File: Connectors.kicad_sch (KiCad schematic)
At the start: 13 parts, among them J4 Conn_01x06, J5 Conn_01x06, U10 TJA1051T/3

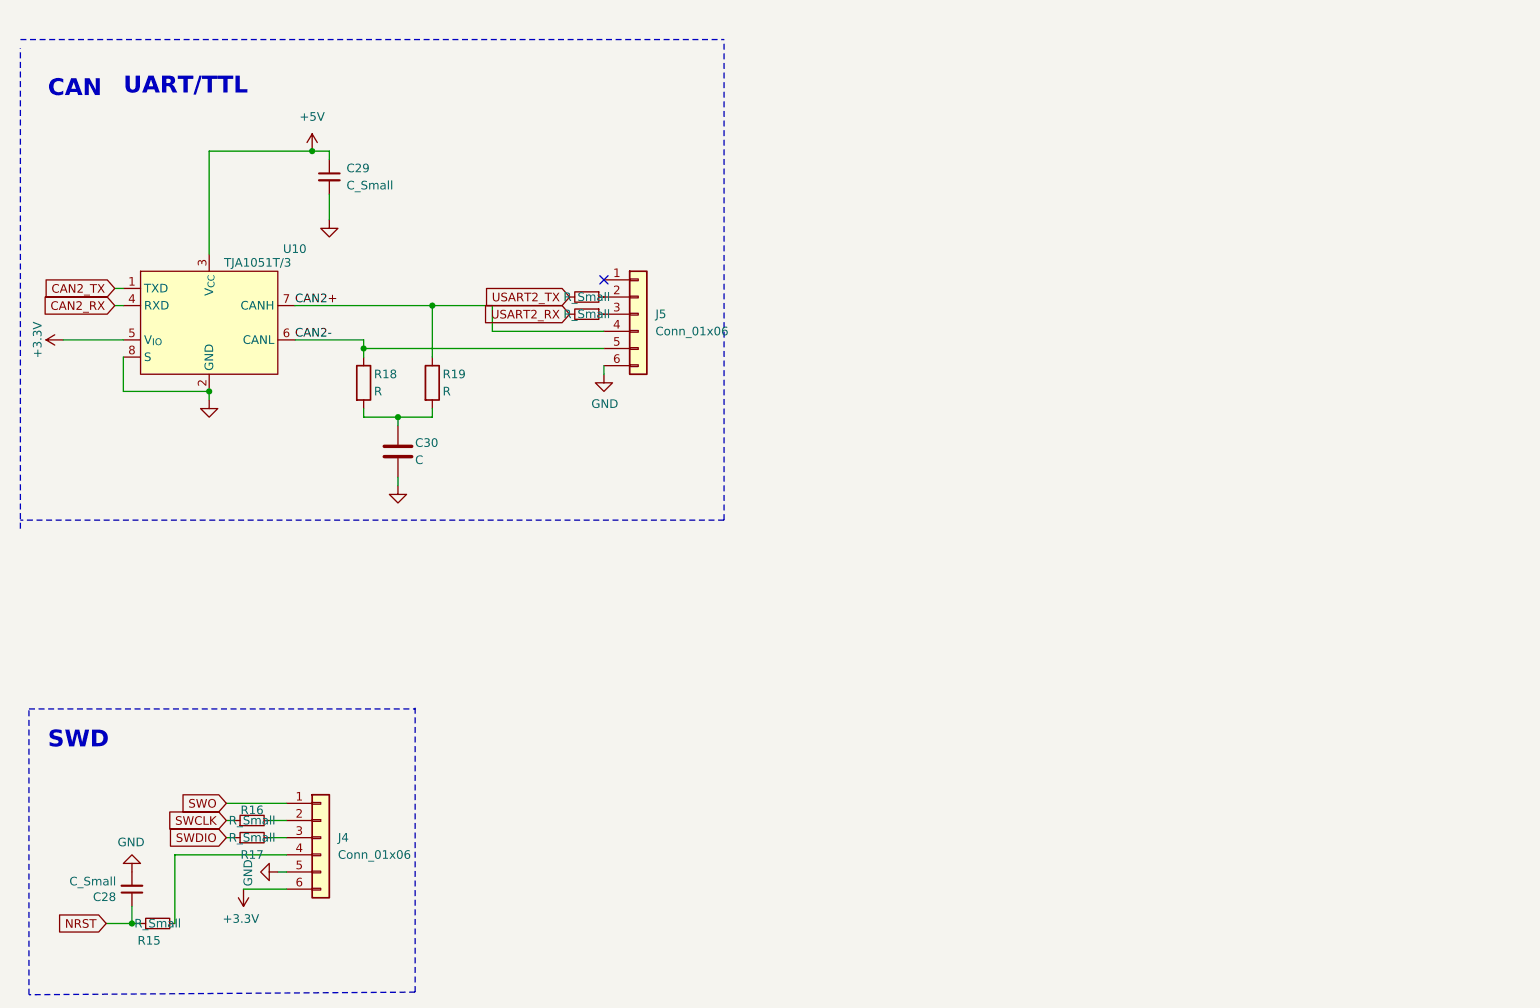
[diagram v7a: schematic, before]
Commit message: update value for capacity and  resistor
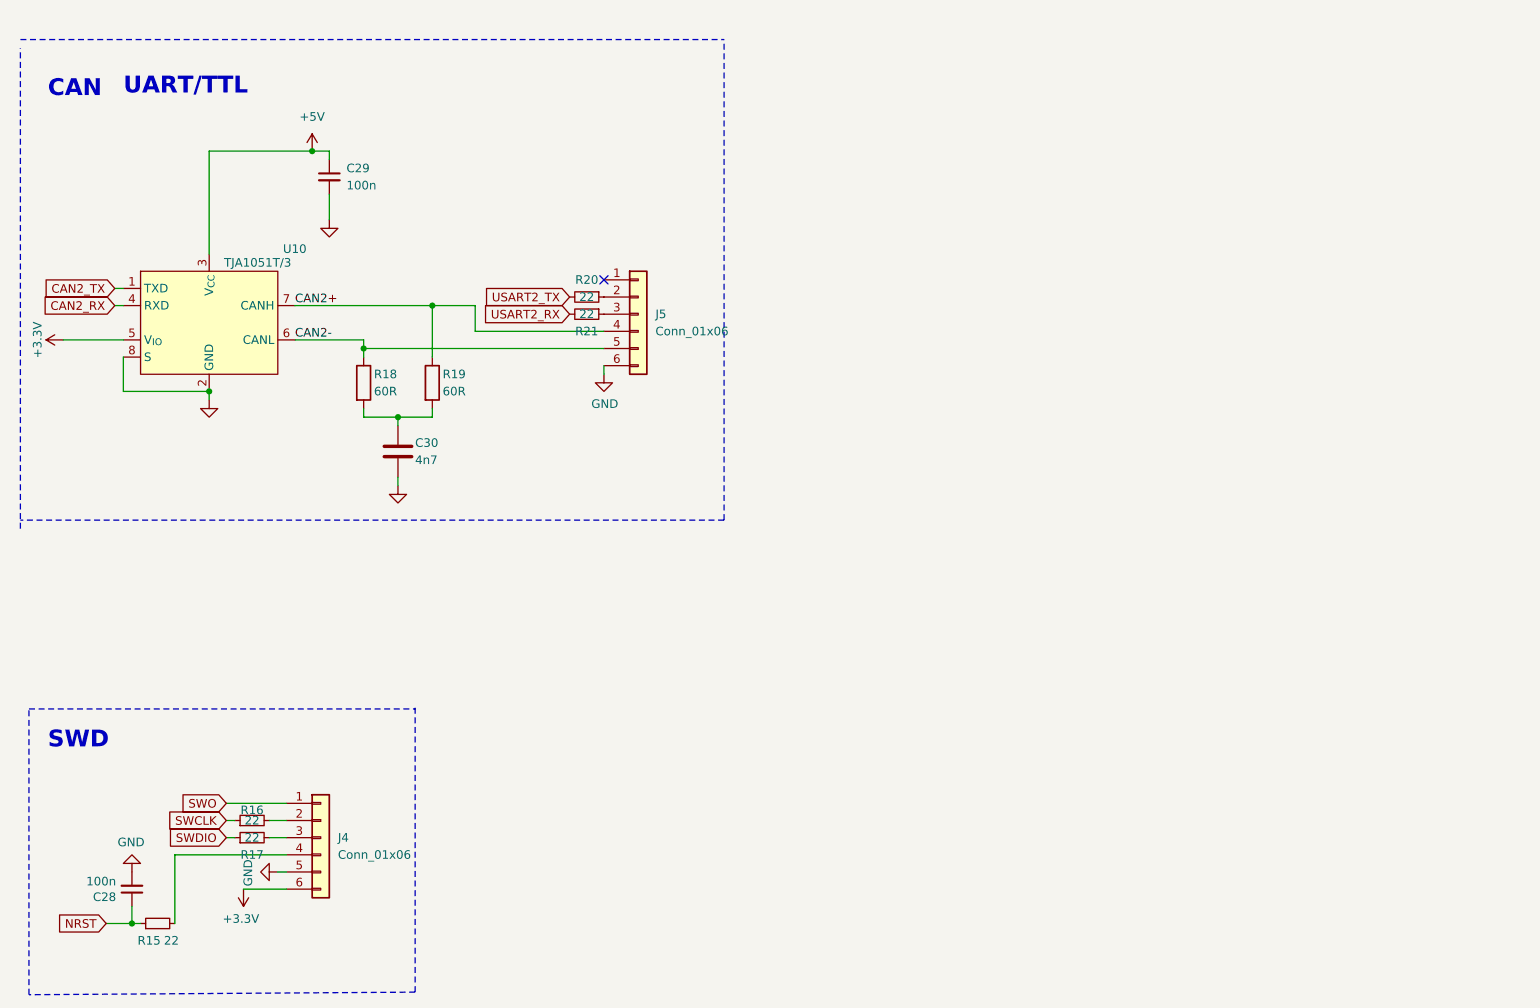
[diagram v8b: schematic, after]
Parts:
- C28, C29: value C_Small -> 100n
- C30: value C -> 4n7
- R15, R16, R17, R20, R21: value R_Small -> 22
- R18, R19: value R -> 60R
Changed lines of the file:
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@@
 	(wire
 		(pts
-			(xy 104.14 63.5) (xy 104.14 67.31)
+			(xy 101.6 63.5) (xy 101.6 67.31)
 		)
 		(stroke
@@
 	(wire
 		(pts
-			(xy 95.25 63.5) (xy 104.14 63.5)
+			(xy 95.25 63.5) (xy 101.6 63.5)
 		)
 		(stroke
@@
 	(wire
 		(pts
-			(xy 104.14 67.31) (xy 120.65 67.31)
+			(xy 101.6 67.31) (xy 120.65 67.31)
 		)
 		(stroke
@@
 					(size 1.27 1.27)
 				)
-				(hide yes)
-			)
-		)
-		(property "Value" "R_Small"
+			)
+		)
+		(property "Value" "22"
 			(at 118.11 62.23 90)
 			(effects
@@
 					(size 1.27 1.27)
 				)
-				(hide yes)
-			)
-		)
-		(property "Value" "R_Small"
+			)
+		)
+		(property "Value" "22"
 			(at 118.11 64.77 90)
 			(effects
@@
 			)
 		)
-		(property "Value" "R_Small"
+		(property "Value" "22"
 			(at 68.58 142.24 90)
 			(effects
@@
 			)
 		)
-		(property "Value" "R_Small"
+		(property "Value" "22"
 			(at 68.58 139.7 90)
 			(effects
@@
 			)
 		)
-		(property "Value" "R_Small"
-			(at 54.61 154.94 90)
+		(property "Value" "22"
+			(at 56.642 157.48 90)
 			(effects
 				(font
@@
 			)
 		)
-		(property "Value" "C_Small"
+		(property "Value" "100n"
 			(at 48.4632 148.717 0)
 			(effects
@@
 			)
 		)
-		(property "Value" "C"
+		(property "Value" "4n7"
 			(at 92.71 86.36 0)
 			(effects
@@
 			)
 		)
-		(property "Value" "R"
+		(property "Value" "60R"
 			(at 86.614 76.2 0)
 			(effects
@@
 			)
 		)
-		(property "Value" "R"
+		(property "Value" "60R"
 			(at 96.774 76.2 0)
 			(effects
@@
 			)
 		)
-		(property "Value" "C_Small"
+		(property "Value" "100n"
 			(at 82.55 45.72 0)
 			(effects
